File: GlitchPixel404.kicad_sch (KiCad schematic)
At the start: 36 parts, among them J1 USB_C_Receptacle_USB2.0_16P, J2 VOLTLINK, J5 Barrel_Jack_Switch, J7 Output, Q1 AONR21357-ES, Q2 MMBT3904, SW1 Reset, SW2 Boot, U1 ESP32-PICO-MINI-02U-N8R2, U2 SN74LVC2T45DCUR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

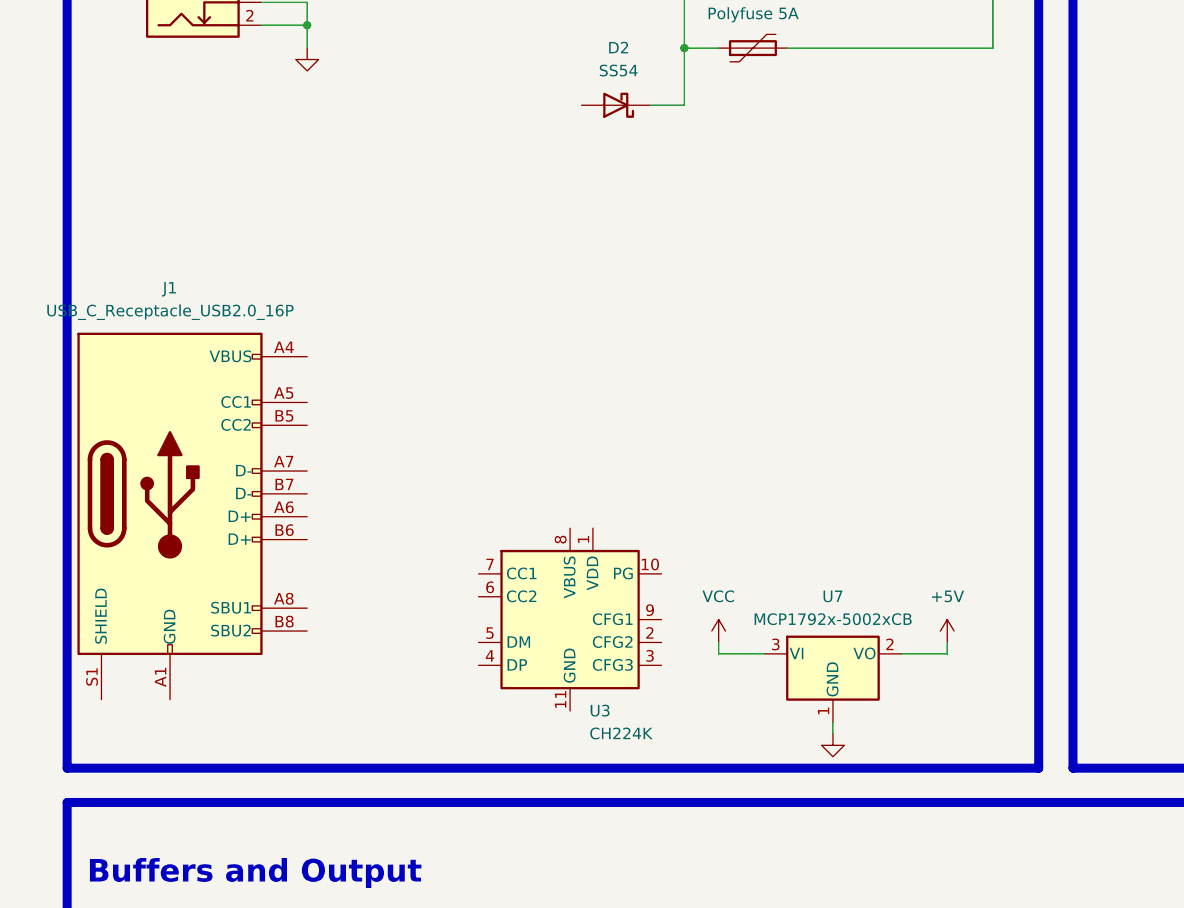
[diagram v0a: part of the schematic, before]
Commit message: Add USB PD Trig Circuit
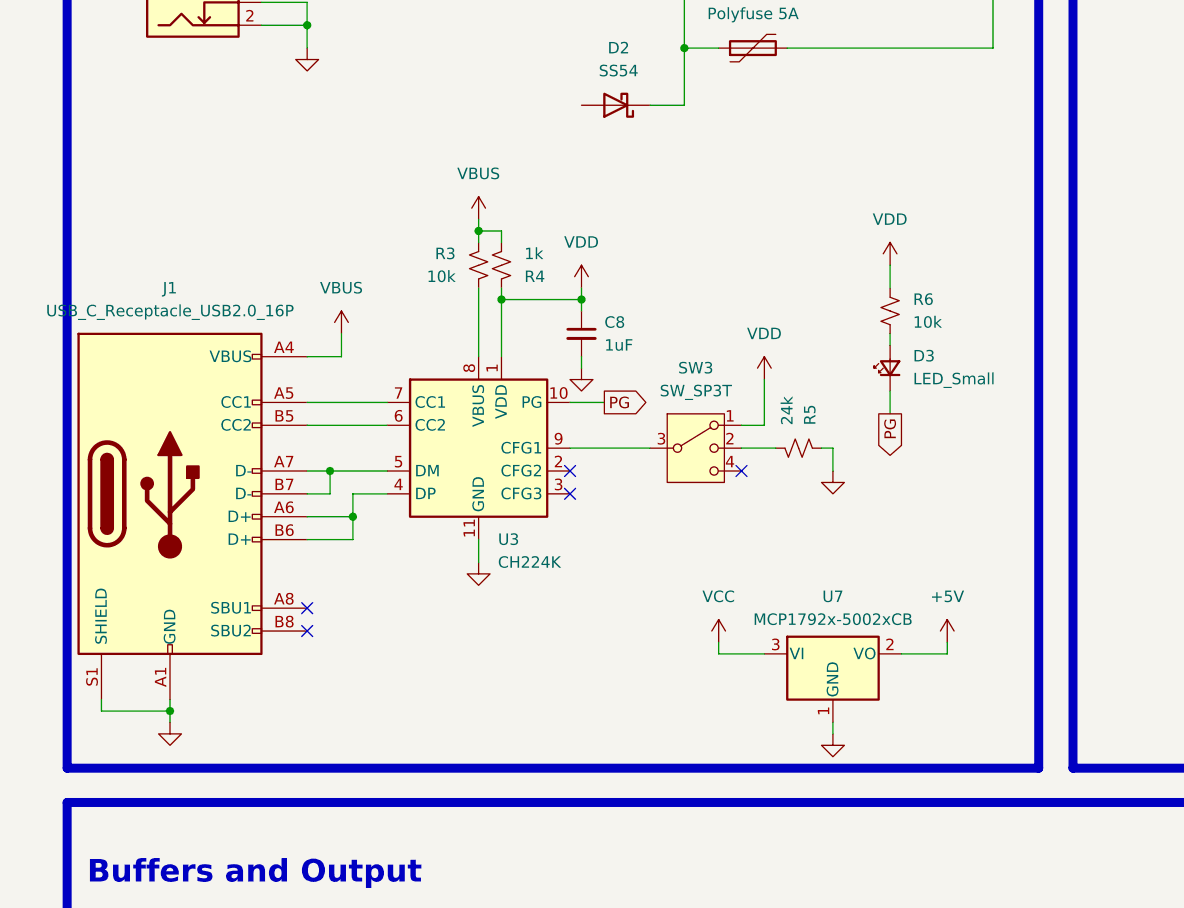
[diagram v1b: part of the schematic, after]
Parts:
- added C8: 1uF, Capacitor_SMD:C_0603_1608Metric, symbol Device:C_Small
- added D3: LED_Small, LED_SMD:LED_0603_1608Metric, symbol Device:LED_Small
- added R3, R6: 10k, Resistor_SMD:R_0603_1608Metric, symbol Device:R_Small_US
- added R4: 1k, Resistor_SMD:R_0603_1608Metric, symbol Device:R_Small_US
- added R5: 24k, Resistor_SMD:R_0603_1608Metric, symbol Device:R_Small_US
- added SW3: SW_SP3T, Button_Switch_SMD:SW_SP3T_PCM13, symbol Switch:SW_SP3T
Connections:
- net GND: now also J1.A1 (GND), J1.A12 (GND), J1.B1 (GND), J1.B12 (GND), J1.S1 (SHIELD), U3.11 (GND), C8.2, R5.1
- net VBUS: now reaches J1.A4 (VBUS), J1.A9 (VBUS), J1.B4 (VBUS), J1.B9 (VBUS)
- net VBUS: now also R3.1, R4.2
- net at J1.A5 (CC1): now also U3.7 (CC1)
- net at J1.A6 (D+): now also J1.B6 (D+), U3.4 (DP)
- net at J1.A7 (D-): now also J1.B7 (D-), U3.5 (DM)
- net at J1.B5 (CC2): now also U3.6 (CC2)
- net VDD: now reaches U3.1 (VDD)
- net VDD: now also C8.1, R4.1, R6.1, SW3.1
- net PG: now reaches U3.10 (PG)
- net PG: now also D3.1 (K)
- net at U3.8 (VBUS): now also R3.2
- net at U3.9 (CFG1): now also SW3.3
- new net: D3.2 (A), R6.2
- new net: R5.2, SW3.2
- no-connect marks 0 -> 5
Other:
- moved on the sheet: U3

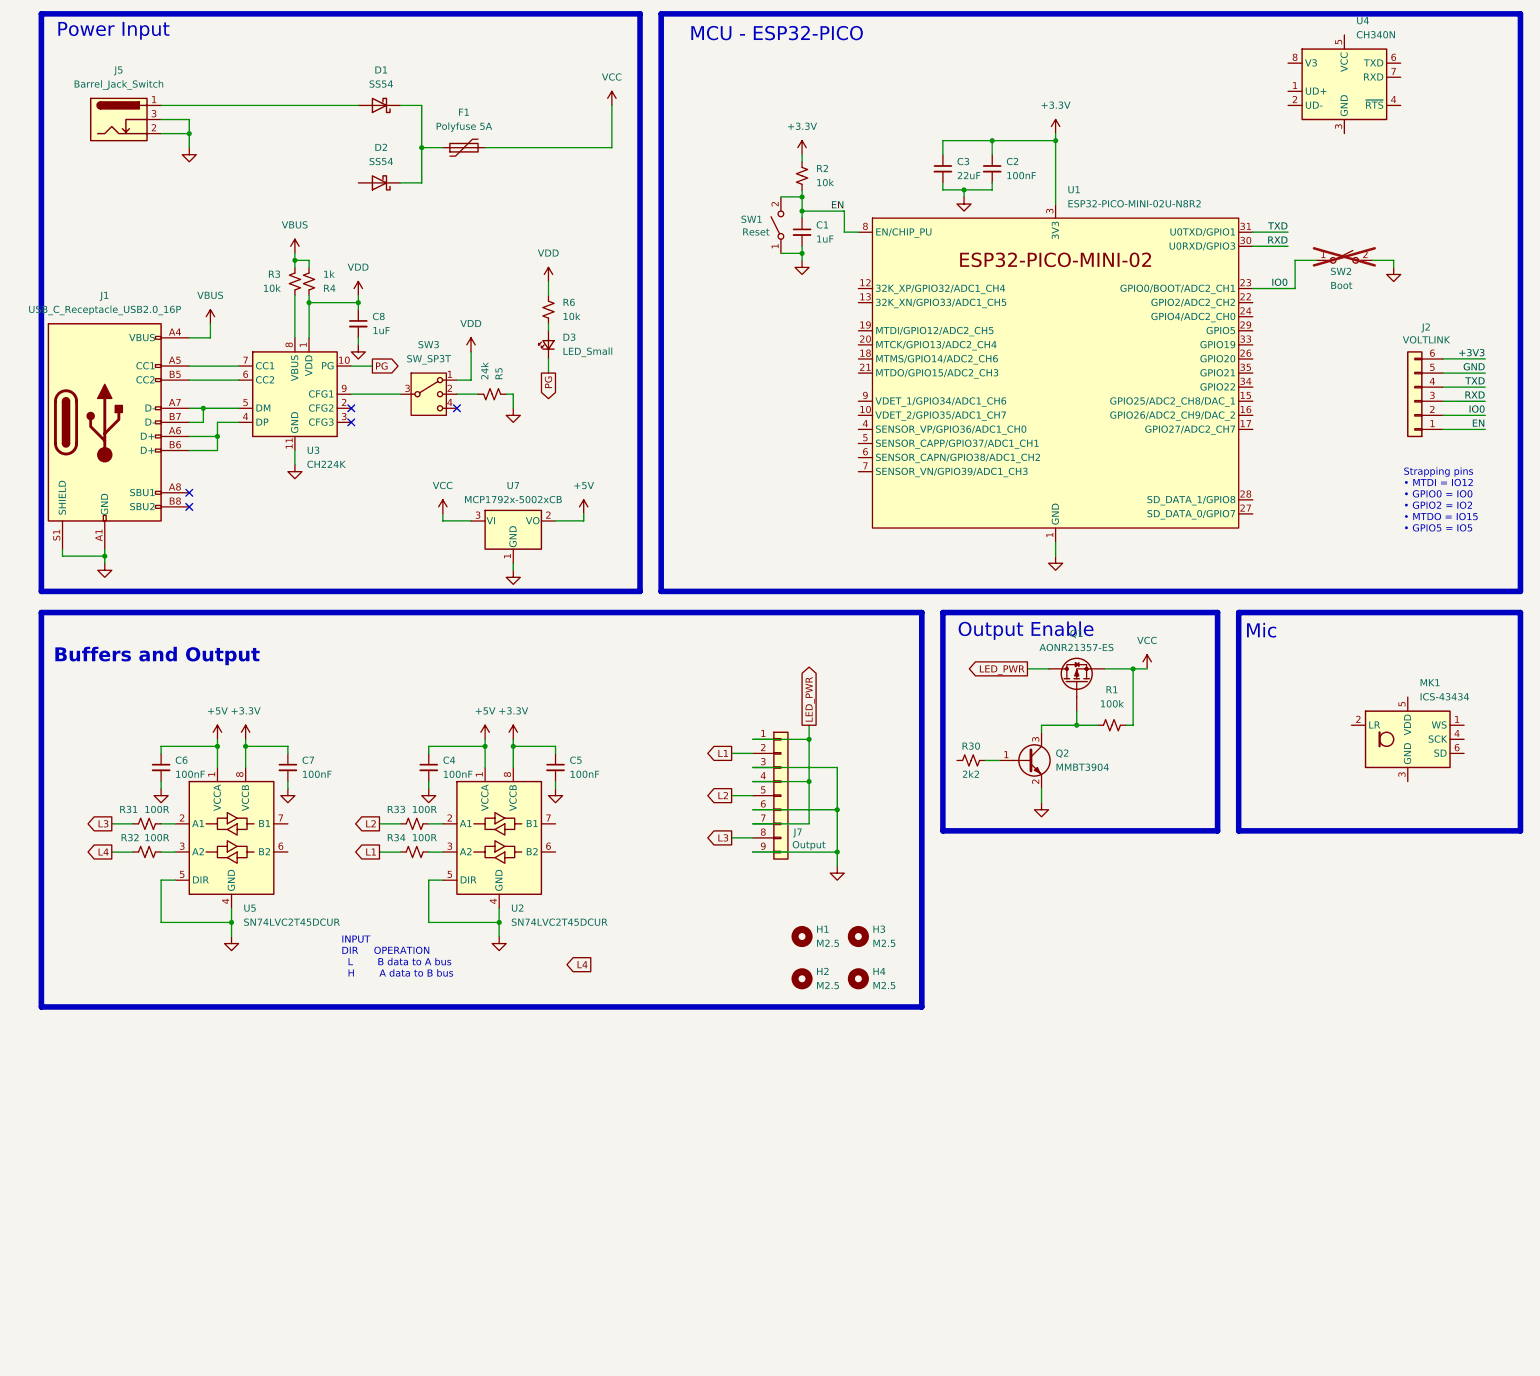
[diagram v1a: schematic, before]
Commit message: Changed buffers to 74LVC2G34 and added datasheets
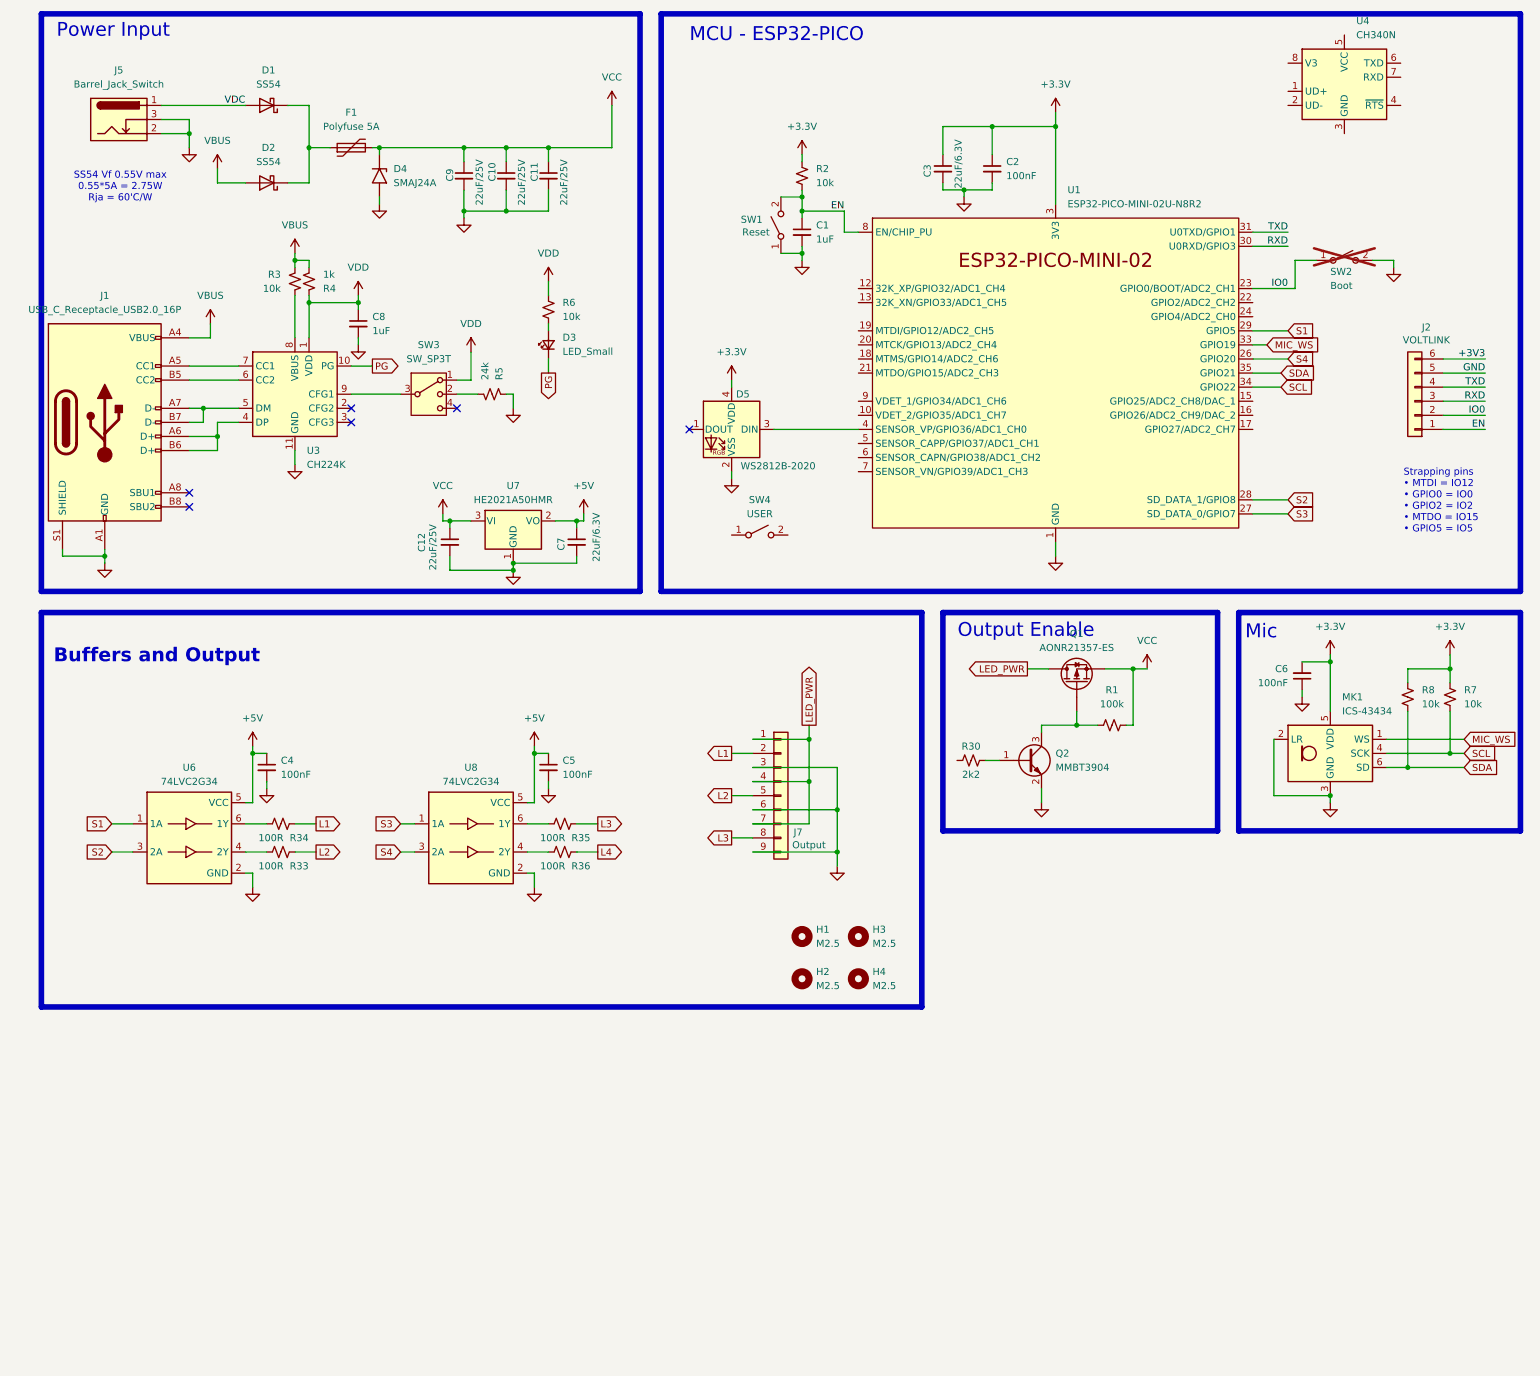
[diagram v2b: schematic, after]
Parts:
- removed R31, R32: 100R, Resistor_SMD:R_0603_1608Metric, symbol Device:R_Small_US
- removed U2, U5: SN74LVC2T45DCUR, Package_SO:VSSOP-8_2.3x2mm_P0.5mm, symbol Logic_LevelTranslator:SN74LVC2T45DCUR
- added C10, C11, C12, C9: 22uF/25V, Capacitor_SMD:C_0805_2012Metric, symbol Device:C_Small
- added D4: SMAJ24A, Diode_SMD:D_SMA, symbol Diode:SMAJ24A
- added D5: WS2812B-2020, LED_SMD:LED_WS2812B-2020_PLCC4_2.0x2.0mm, symbol LED:WS2812B-2020
- added R35, R36: 100R, Resistor_SMD:R_0603_1608Metric, symbol Device:R_Small_US
- added R7, R8: 10k, Resistor_SMD:R_0603_1608Metric, symbol Device:R_Small_US
- added SW4: USER, symbol Switch:SW_SPST
- added U6, U8: 74LVC2G34, Package_TO_SOT_SMD:SOT-363_SC-70-6, symbol Inventel:74LVC2G34
- C3: value 22uF -> 22uF/6.3V
- C7: value 100nF -> 22uF/6.3V; footprint Capacitor_SMD:C_0402_1005Metric -> Capacitor_SMD:C_0603_1608Metric; LCSC C1525 -> C59461; MPN CL05B104KO5NNNC -> CL10A226MQ8NRNC; Volt 16V -> 6.3V
- U7: value MCP1792x-5002xCB -> HE2021A50HMR; LCSC (none) -> C711948
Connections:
- net +3.3V: now also C6.2, MK1.5 (VDD), D5.4 (VDD), R7.1, R8.1; no longer C5.1, C7.1
- net +5V: now also C5.1, C7.1, U6.5 (VCC), U8.5 (VCC); no longer C6.1
- net GND: now also C6.1, MK1.2 (LR), MK1.3 (GND), C10.2, C11.2, C12.2, C9.2, D4.2 (A2), D5.2 (VSS), U6.2 (GND), U8.2 (GND); no longer C6.2
- net L3: now also R35.1
- net L4: now also R36.1
- net VBUS: now also D2.2 (A)
- net VCC: now also C10.1, C11.1, C12.1, C9.1, D4.1 (A1)
- net MIC_WS: now reaches MK1.1 (WS)
- net MIC_WS: now also U1.33 (GPIO19)
- net SCL: now reaches MK1.4 (SCK)
- net SCL: now also U1.34 (GPIO22), R7.2
- net SDA: now reaches MK1.6 (SD)
- net SDA: now also U1.35 (GPIO21), R8.2
- net at R33.2: now also U6.4 (2Y)
- net at R34.2: now also U6.6 (1Y)
- net VDC: now reaches D1.2 (A), J5.1
- net S4: now reaches U1.26 (GPIO20)
- net S4: now also U8.3 (2A)
- net S3: now reaches U1.27 (SD_DATA_0/GPIO7)
- net S3: now also U8.1 (1A)
- net S2: now reaches U1.28 (SD_DATA_1/GPIO8)
- net S2: now also U6.3 (2A)
- net S1: now reaches U1.29 (GPIO5)
- net S1: now also U6.1 (1A)
- net at U1.4 (SENSOR_VP/GPIO36/ADC1_CH0): now also D5.3 (DIN)
- new net: R36.2, U8.4 (2Y)
- new net: R35.2, U8.6 (1Y)
- no-connect marks 5 -> 6
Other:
- note added: "SS54 Vf 0.55V max 0.55*5A = 2.75W Rja = 60'C/W"
- note removed: "INPUT DIR OPERATION L B data to A bus H A data to B bus"
- moved on the sheet: C4, D1, D2, F1, MK1, R33, R34

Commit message: Added 3v3 DCDC
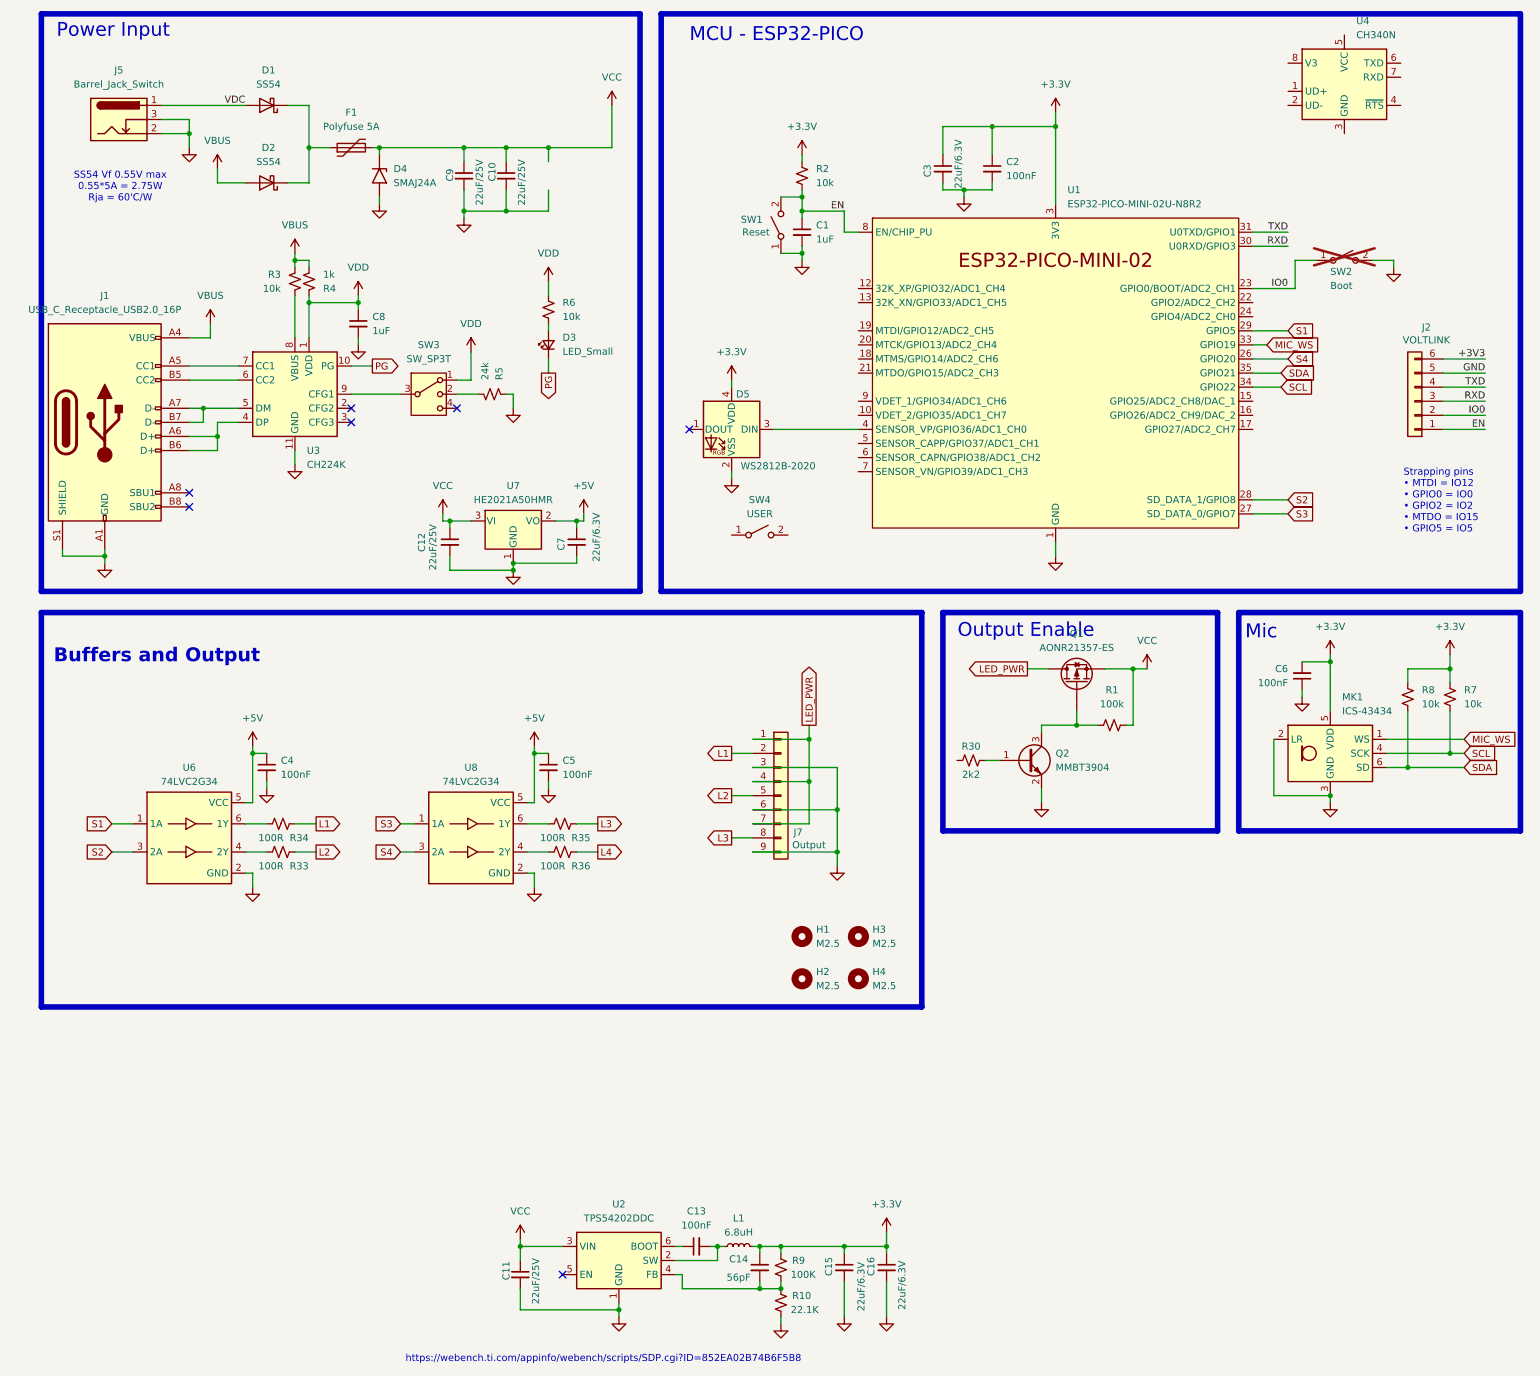
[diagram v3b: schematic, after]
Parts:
- added C13: 100nF, Capacitor_SMD:C_0402_1005Metric, symbol Device:C_Small
- added C14: 56pF, Capacitor_SMD:C_0402_1005Metric, symbol Device:C_Small
- added C15, C16: 22uF/6.3V, Capacitor_SMD:C_0603_1608Metric, symbol Device:C_Small
- added L1: 6.8uH, symbol Device:L_Small
- added R10: 22.1K, Resistor_SMD:R_0402_1005Metric, symbol Device:R_Small_US
- added R9: 100K, Resistor_SMD:R_0402_1005Metric, symbol Device:R_Small_US
- added U2: TPS54202DDC, Package_TO_SOT_SMD:SOT-23-6, symbol Regulator_Switching:TPS54202DDC
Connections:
- net +3.3V: now also C14.1, C15.1, C16.1, L1.2, R9.1
- net GND: now also C15.2, C16.2, R10.2, U2.1 (GND)
- net VCC: now also U2.3 (VIN)
- new net: C14.2, R10.1, R9.2, U2.4 (FB)
- new net: C13.2, L1.1, U2.2 (SW)
- new net: C13.1, U2.6 (BOOT)
- no-connect marks 6 -> 7
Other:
- note added: "https://webench.ti.com/appinfo/webench/scripts/SDP.cgi?ID=852EA02B74B6F5B8"
- moved on the sheet: C11
